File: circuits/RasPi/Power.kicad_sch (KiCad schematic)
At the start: 81 parts, among them IC1 DCDC_MPM3620A, J10 Conn_01x02_Male, J11 Conn_01x02_Male, J12 Conn_01x02_Male, J13 Conn_01x02_Male, J6 USB_C_Receptacle_USB2.0, J9 Conn_01x02_Male, Q16 SSM6J808R, Q17 SSM6J808R, Q18 SSM3J332R, Q19 S8550, Q2 BSS138, Q20 SSM3J332R, Q21 S8550, Q23 S8550, Q24 SSM3J332R, Q25 S8550, Q3 SSM3J332R, Q4 BSS138, SW1 SW_SPDT_White

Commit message: 無線&UI完成？
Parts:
- added J12, J13, J14: Conn_01x02_Male, Connector_Molex:Molex_SPOX_5267-02A_1x02_P2.50mm_Vertical, symbol Connector:Conn_01x02_Male
- renumbered C40 to C19, C1 to C20, C23 to C21, C2 to C22, C3 to C23, C4 to C24, C5 to C25, C32 to C26, C6 to C27, C33 to C28, C23 to C29, C8 to C30, C37 to C31, C25 to C32, C38 to C33, C26 to C34, C39 to C35, D5 to D10, D6 to D11, D1 to D4, D8 to D5, D2 to D6, D3 to D7, D4 to D8, J12 to J10, J13 to J11, J9 to J7, J10 to J8, J11 to J9, Q2 to Q10, Q3 to Q11, Q17 to Q12, Q4 to Q13, Q16 to Q14, Q23 to Q15, Q24 to Q16, Q25 to Q17, Q18 to Q6, Q19 to Q7, Q20 to Q8, Q21 to Q9, R64 to R42, R65 to R43, R76 to R44, R3 to R45, R91 to R46, R92 to R47, R93 to R48, R94 to R49, R4 to R50, R5 to R51, R6 to R52, R95 to R53, R8 to R54, R96 to R55, R7 to R56, R10 to R57, R9 to R58, R11 to R59, R1 to R60, R12 to R61, R2 to R62, R99 to R63, R13 to R64, R100 to R65, R14 to R66, R15 to R67, R16 to R68, R17 to R69, R18 to R70, R19 to R71, R20 to R72, R65 to R73, SW1 to SW4, TP3 to TP1, TP1 to TP2, TP2 to TP3
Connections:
- net +BATT: now also J12.2 (Pin_2), J13.2 (Pin_2), J14.2 (Pin_2)
- net GND: now also J12.1 (Pin_1), J13.1 (Pin_1), J14.1 (Pin_1)
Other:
- note added: "三端子を新しく選定したのにする"
- note removed: "三端子を新しく選定したのにする 電源直付けのための穴を設定する 電源平滑コンデンサは基板設計の時に良い感じに数調整"

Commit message: ラズパイ基板とか
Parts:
- removed C26, C28, C31, C33, C35: 470uF, symbol Device:C_Polarized
- removed J10, J11, J12, J13, J14, J7, J8, J9: Conn_01x02_Male, Connector_Molex:Molex_SPOX_5267-02A_1x02_P2.50mm_Vertical, symbol Connector:Conn_01x02_Male
- R71, R72, R73: value 2k -> 1k
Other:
- note removed: "Conn to EachBoard"
- note removed: "Conn to Power"

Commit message: PDFプロット
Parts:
- removed IC1: DCDC_MPM3620A, MyLibrary:DCDC_MPM3620A, symbol MyLibrary:DCDC_MPM3620A
- removed Q11: SSM3J332R, Package_TO_SOT_SMD:SOT-23W, symbol Device:Q_PMOS_GSD
- added C47: 4700pF, Capacitor_SMD:C_0603_1608Metric, symbol Device:C
- added C48, C50: 47uF, Capacitor_SMD:C_0805_2012Metric, symbol Device:C
- added C49: 100uF, Capacitor_SMD:C_0805_2012Metric, symbol Device:C
- added C51: 0.1uF, Capacitor_SMD:C_0603_1608Metric, symbol Device:C
- added C52: 0.1uF, Capacitor_SMD:C_0402_1005Metric, symbol Device:C
- added D16, D18: D_Zener, Diode_SMD:D_SOD-323_HandSoldering, symbol Device:D_Zener
- added D17, D19: SS2040FL, Diode_SMD:D_SOD-123, symbol Device:D_Schottky
- added J4: Conn_01x02_Pin, symbol Connector:Conn_01x02_Pin
- added L2, L3: 2.2uH, MyLibrary:Inductor_CDPH4D19F, symbol Device:L
- added R119: 200k, Resistor_SMD:R_0402_1005Metric, symbol Device:R
- added R121: 53.6k, Resistor_SMD:R_0402_1005Metric, symbol Device:R
- added R122: 10k, Resistor_SMD:R_0402_1005Metric, symbol Device:R
- added U13: TPS54560BDDA, Package_SO:Texas_R-PDSO-G8_EP2.95x4.9mm_Mask2.4x3.1mm_ThermalVias, symbol Regulator_Switching:TPS54560BDDA
- added U15: TPS61022, Package_DFN_QFN:Texas_RWU0007A_VQFN-7_2x2mm_P0.5mm, symbol Converter_DCDC:TPS61022
- added U16: AZ1084CD-3.3, Package_TO_SOT_SMD:TO-252-2, symbol Regulator_Linear:AMS1117CD-3.3
- added U17: M51957B, Package_SO:SOP-8_3.9x4.9mm_P1.27mm, symbol Voltage_Supervisor:M51957B
- C20: value 10uF -> 47uF; footprint Capacitor_SMD:C_1206_3216Metric -> Capacitor_SMD:C_0805_2012Metric
- C22: value 22uF -> 1uF; footprint Capacitor_SMD:C_0805_2012Metric -> Capacitor_SMD:C_0603_1608Metric
- R45: value 200k -> 10k
- R50: value 100k -> 10k
- R51: value 12k -> 53.6k
- R52: value 2.2k -> 10k
- R54: value 10k -> 75k; footprint Resistor_SMD:R_0402_1005Metric -> Resistor_SMD:R_0603_1608Metric
- R57: value 10k -> 5.1k; footprint Resistor_SMD:R_0402_1005Metric -> Resistor_SMD:R_0603_1608Metric
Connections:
- net +3.3V: now also U16.2 (VO)
- net +5V: now also C52.2, U16.3 (VI), U17.7 (VCC)
- net GND: now also R57.2, C47.1, C48.2, C49.2, C50.2, C52.1, D17.2 (A), D18.2 (A), J4.1 (Pin_1), R119.1, R122.1, U13.7 (GND), U13.9 (GND), U15.1 (GND), U16.1 (GND), U17.4 (GND); no longer Q10.2 (S), R57.1
- net VCC: now also C50.1, U13.2 (VIN); no longer C20.1, R45.2
- net VDD: now also R54.2
- net VSYS: now also C22.1, D4.2 (A), Q10.3 (D), R50.2, R51.2, C48.1, C49.1, D19.1 (K), L2.2, R121.2, U15.3 (VOUT), U15.5 (EN), U15.7 (VIN); no longer R57.2
- net Vout: no longer C22.1, D4.2 (A), R51.2, R54.1
- net FB_Boost: now reaches R51.1, R52.2
- net FB_Boost: now also U15.4 (FB)
- net at R45.1: now also Q10.2 (S)
- net PG: no longer names the net of Q10.1 (G), R50.1
- net PG: now also D16.1 (K), D18.1 (K)
- new net: R54.1, R57.1, U17.2 (IN)
- new net: C47.2, U17.5 (Cdelay)
- new net: C51.2, D17.1 (K), L2.1, U13.8 (SW)
- new net: L3.1, U15.2 (SW)
- new net: C51.1, U13.1 (BOOT)
- new net: R119.2, U13.4 (RT/CLK)
- new net Cap: C20.1, D16.2 (A), D19.2 (A), J4.2 (Pin_2), L3.2, R45.2
- new net FB_Buck: R121.1, R122.2, U13.5 (FB)
- new net UV_SHDN: U17.6 (OUT)
- no-connect marks 11 -> 9
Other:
- note added: "定電流回路"
- note added: "昇圧回路"
- note added: "電圧監視"
- note added: "電気二重層キャパシタへ"
- moved on the sheet: C19, C21, C23, C24, C25, C27, C29, C30, C32, C34, D10, D11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

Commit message: panelフットプリント配置
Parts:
- removed C19: 10uF, Capacitor_SMD:C_0805_2012Metric, symbol Device:C
- removed C20, C48: 47uF, Capacitor_SMD:C_0805_2012Metric, symbol Device:C
- removed C22: 1uF, Capacitor_SMD:C_0603_1608Metric, symbol Device:C
- removed D19: SS2040FL, Diode_SMD:D_SOD-123, symbol Device:D_Schottky
- removed J6: USB_C_Receptacle_USB2.0, Connector_USB:USB_C_Receptacle_G-Switch_GT-USB-7010ASV, symbol Connector:USB_C_Receptacle_USB2.0
- removed L3: 2.2uH, MyLibrary:Inductor_CDPH4D19F, symbol Device:L
- removed R42, R43: 5.1k, Resistor_SMD:R_0402_1005Metric, symbol Device:R
- removed R51: 53.6k, Resistor_SMD:R_0402_1005Metric, symbol Device:R
- removed R52: 10k, Resistor_SMD:R_0402_1005Metric, symbol Device:R
- removed U15: TPS61022, Package_DFN_QFN:Texas_RWU0007A_VQFN-7_2x2mm_P0.5mm, symbol Converter_DCDC:TPS61022
- added C55, C57: 47uF, Capacitor_SMD:C_0805_2012Metric, symbol Device:C
- added C56: 1uF, Capacitor_SMD:C_0603_1608Metric, symbol Device:C
- added D27: SS2040FL, Diode_SMD:D_SOD-123, symbol Device:D_Schottky
- added L4: 2.2uH, MyLibrary:Inductor_CDPH4D19F, symbol Device:L
- added R100: 10k, Resistor_SMD:R_0402_1005Metric, symbol Device:R
- added R99: 53.6k, Resistor_SMD:R_0402_1005Metric, symbol Device:R
- added U19: DCDC_TPS61023, MyLibrary:DCDC_TPS61023, symbol MyLibrary:DCDC_TPS61023
- U16: value AZ1084CD-3.3 -> AZ1117CH-3.3; footprint Package_TO_SOT_SMD:TO-252-2 -> Package_TO_SOT_SMD:SOT-223-3_TabPin2
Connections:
- net Cap: now also C55.1, D27.2 (A), L4.2
- net FB_Boost: now also R100.2, R99.1, U19.1 (FB)
- net GND: now also C55.2, C56.2, C57.2, R100.1, U19.4 (GND)
- net VSYS: now also C56.1, C57.1, D27.1 (K), R99.2, U19.2 (EN), U19.3 (VIN), U19.6 (VOUT)
- new net: L4.1, U19.5 (SW)
- no-connect marks 9 -> 3
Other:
- note added: "三端子を新しく選定したのにする 昇圧回路のFB電圧をちょっと低く設定する"
- note removed: "USB-C"
- note removed: "三端子を新しく選定したのにする"
- moved on the sheet: C21, C24, C25, C47, C52, D5, D8, Q6, Q7, Q8, Q9, R44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

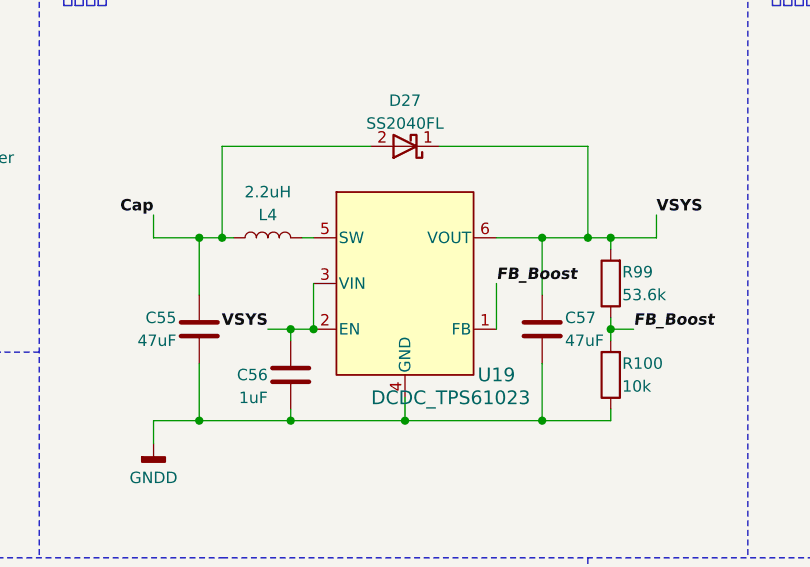
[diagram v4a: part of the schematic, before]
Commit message: シンボル・フットプリントMyLib->TomoshibiLib置き換え
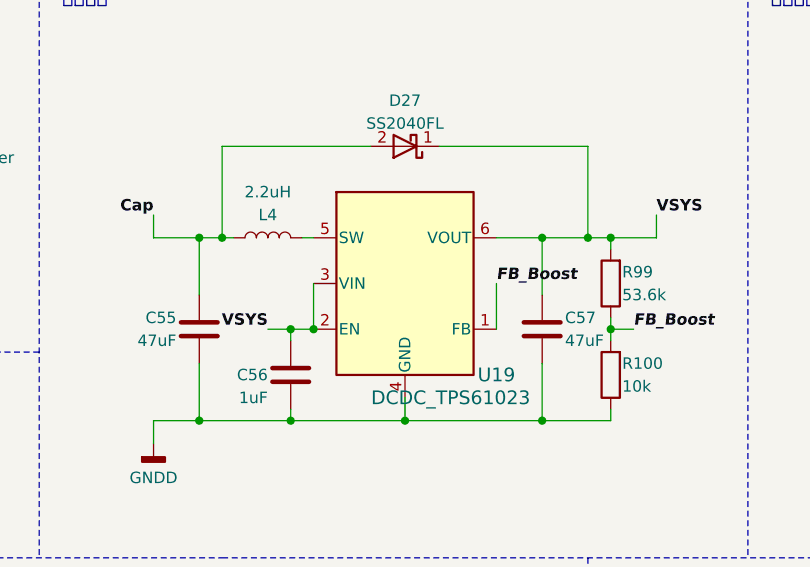
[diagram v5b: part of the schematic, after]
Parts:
- L1: footprint MyLibrary:Inductor_CDPH4D19F -> TomoshibiLibrary:Inductor_CDPH4D19F
- L2, L4: footprint MyLibrary:Inductor_CDPH4D19F -> (none)
- Q12, Q14: footprint MyLibrary:Package_TSOP6F -> TomoshibiLibrary:Package_TSOP6F
- SW4: footprint MyLibrary:SW_Slide_SPDT_White -> TomoshibiLibrary:SW_Slide_SPDT_White
- U17: symbol Voltage_Supervisor:M51957B -> TomoshibiLibrary:Power_Supervisor_M51957B
- U19: footprint MyLibrary:DCDC_TPS61023 -> TomoshibiLibrary:DCDC_TPS61023; symbol MyLibrary:DCDC_TPS61023 -> TomoshibiLibrary:DCDC_TPS61023
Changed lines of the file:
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@@
       (effects (font (size 1.27 1.27)))
     )
-    (property "Footprint" "MyLibrary:Inductor_CDPH4D19F" (at 129.54 71.12 0)
+    (property "Footprint" "TomoshibiLibrary:Inductor_CDPH4D19F" (at 129.54 71.12 0)
       (effects (font (size 1.27 1.27)) hide)
     )
@@
       (effects (font (size 1.27 1.27)))
     )
-    (property "Footprint" "MyLibrary:Inductor_CDPH4D19F" (at 210.82 147.32 0)
+    (property "Footprint" "" (at 210.82 147.32 0)
       (effects (font (size 1.27 1.27)) hide)
     )
@@
     )
   )
-  (symbol (lib_id "MyLibrary:DCDC_TPS61023") (at 226.06 152.4 0) (unit 1)
+  (symbol (lib_id "TomoshibiLibrary:DCDC_TPS61023") (at 226.06 152.4 0) (unit 1)
     (in_bom yes) (on_board yes) (dnp no)
     (property "Reference" "U19" (at 236.22 162.56 0)
@@
       (effects (font (size 1.524 1.524)))
     )
-    (property "Footprint" "MyLibrary:DCDC_TPS61023" (at 223.52 124.46 0)
+    (property "Footprint" "TomoshibiLibrary:DCDC_TPS61023" (at 223.52 124.46 0)
       (effects (font (size 1.27 1.27) italic) hide)
     )
@@
       (effects (font (size 1.27 1.27)))
     )
-    (property "Footprint" "MyLibrary:SW_Slide_SPDT_White" (at 86.36 40.64 0)
+    (property "Footprint" "TomoshibiLibrary:SW_Slide_SPDT_White" (at 86.36 40.64 0)
       (effects (font (size 1.27 1.27)) hide)
     )
@@
       (effects (font (size 1.27 1.27)))
     )
-    (property "Footprint" "MyLibrary:Inductor_CDPH4D19F" (at 104.14 149.86 0)
+    (property "Footprint" "" (at 104.14 149.86 0)
       (effects (font (size 1.27 1.27)) hide)
     )
@@
       (effects (font (size 1.27 1.27)))
     )
-    (property "Footprint" "MyLibrary:Package_TSOP6F" (at 96.52 68.58 0)
+    (property "Footprint" "TomoshibiLibrary:Package_TSOP6F" (at 96.52 68.58 0)
       (effects (font (size 1.27 1.27)) (justify left) hide)
     )
@@
       (effects (font (size 1.27 1.27)))
     )
-    (property "Footprint" "MyLibrary:Package_TSOP6F" (at 71.12 68.58 0)
+    (property "Footprint" "TomoshibiLibrary:Package_TSOP6F" (at 71.12 68.58 0)
       (effects (font (size 1.27 1.27)) (justify left) hide)
     )
@@
     )
   )
-  (symbol (lib_id "Voltage_Supervisor:M51957B") (at 91.44 215.9 0) (unit 1)
+  (symbol (lib_id "TomoshibiLibrary:Power_Supervisor_M51957B") (at 91.44 215.9 0) (unit 1)
     (in_bom yes) (on_board yes) (dnp no)
     (property "Reference" "U17" (at 99.06 205.74 0)

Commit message: 更新
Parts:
- removed Q10, Q13: BSS138, Package_TO_SOT_SMD:SOT-23, symbol Device:Q_NMOS_GSD
- removed Q16: SSM3J332R, Package_TO_SOT_SMD:SOT-23W, symbol Device:Q_PMOS_GSD
- added Q11: 2N7002, Package_TO_SOT_SMD:SOT-23, symbol Transistor_FET:2N7002
- added Q16: SSM6J808R, Package_SO:TSOP-6_1.65x3.05mm_P0.95mm, symbol Transistor_FET:PMN48XP
- J4: footprint (none) -> Connector_JST:JST_XH_B2B-XH-AM_1x02_P2.50mm_Vertical
- L1: value 22uH -> 1uH; footprint TomoshibiLibrary:Inductor_CDPH4D19F -> Inductor_SMD:L_0603_1608Metric
- Q12, Q14: footprint TomoshibiLibrary:Package_TSOP6F -> Package_SO:TSOP-6_1.65x3.05mm_P0.95mm
- R100: value 10k -> 1.8k; footprint Resistor_SMD:R_0402_1005Metric -> Resistor_SMD:R_0603_1608Metric
- R99: value 53.6k -> 13k; footprint Resistor_SMD:R_0402_1005Metric -> Resistor_SMD:R_0603_1608Metric
- SW4: value SW_SPDT_White -> SW_SPDT
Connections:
- net +5V: now also Q16.1 (D), Q16.2 (D), Q16.5 (D), Q16.6 (D)
- net GND: now also Q11.2 (S)
- net PowerSW: now also Q11.1 (G)
- net VSYS: now also Q16.4 (S)
- net at R61.2: now also Q11.3 (D)
- net at Q17.3 (C), R65.2: now also Q16.3 (G)
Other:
- note added: "スライドスイッチの色分けとか、スイッチの区別を見直す 電源は白スライド"

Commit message: raspi基板回路図
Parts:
- removed C47: 4700pF, Capacitor_SMD:C_0603_1608Metric, symbol Device:C
- removed C56: 1uF, Capacitor_SMD:C_0603_1608Metric, symbol Device:C
- removed D16, D18: D_Zener, Diode_SMD:D_SOD-323_HandSoldering, symbol Device:D_Zener
- removed R45, R50: 10k, Resistor_SMD:R_0402_1005Metric, symbol Device:R
- added C10, C16, C17: 10uF, Capacitor_SMD:C_1206_3216Metric, symbol Device:C
- added C18, C26, C66, C67, C9: 100uF, Capacitor_SMD:C_1206_3216Metric, symbol Device:C
- added C65: 4.7nF, Capacitor_SMD:C_0402_1005Metric, symbol Device:C
- added C68, C71: 10uF, Capacitor_SMD:C_0805_2012Metric, symbol Device:C
- added C69: C, Resistor_SMD:R_0603_1608Metric, symbol Device:C
- added C70: 15pF, Capacitor_SMD:C_0402_1005Metric, symbol Device:C
- added Q31: MTP4835I3, Package_TO_SOT_SMD:TO-252-2, symbol Device:Q_PMOS_GDS
- added R116: 22k, Resistor_SMD:R_0402_1005Metric, symbol Device:R
- added R124: 100k, Resistor_SMD:R_0402_1005Metric, symbol Device:R
- added R125: 0.1, symbol Device:R
- added R126, R127: R, Resistor_SMD:R_0603_1608Metric, symbol Device:R
- added R128: 200, Resistor_SMD:R_0402_1005Metric, symbol Device:R
- added R129: 5.1k, Resistor_SMD:R_0402_1005Metric, symbol Device:R
- added R43: 2k, Resistor_SMD:R_0402_1005Metric, symbol Device:R
- added U21: 74AHC1G02, Package_TO_SOT_SMD:SOT-23-5, symbol 74xGxx:74AHC1G02
- added U22: NJM2732, symbol Amplifier_Operational:LM7332
- C49: footprint Capacitor_SMD:C_0805_2012Metric -> Capacitor_SMD:C_1206_3216Metric
- C50: value 47uF -> 15pF; footprint Capacitor_SMD:C_0805_2012Metric -> Capacitor_SMD:C_0402_1005Metric
- C51: footprint Capacitor_SMD:C_0603_1608Metric -> Capacitor_SMD:C_0402_1005Metric
- C55: value 47uF -> 10uF
- C57: value 47uF -> 10nF; footprint Capacitor_SMD:C_0805_2012Metric -> Capacitor_SMD:C_0402_1005Metric
- D17: value SS2040FL -> MA10EB045; footprint Diode_SMD:D_SOD-123 -> Diode_SMD:Vishay_SMPA
- L2: value 2.2uH -> 3.3uH; footprint (none) -> TomoshibiLibrary:Inductor_ECS-MPIL0530
- L4: value 2.2uH -> 1uH; footprint (none) -> Inductor_SMD:L_1210_3225Metric
- R119: value 200k -> 100k
- R121: value 53.6k -> 22k
- R122: value 10k -> 2.2k
- R54: value 75k -> 100k
- R57: value 5.1k -> 7.5k
- SW4: footprint TomoshibiLibrary:SW_Slide_SPDT_White -> TomoshibiLibrary:SW_Slide_SPDT_IS-1235-G
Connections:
- net Cap: now also C55.2, U19.3 (VIN), C68.2, Q31.2 (D), R124.2; no longer C55.1
- net FB_Boost: now also C57.2
- net FB_Buck: now also R43.2; no longer R122.2
- net GND: now also C55.1, R122.2, C10.2, C16.2, C17.2, C18.2, C26.2, C65.2, C66.2, C67.2, C68.1, C70.2, C71.1, C9.2, R129.1, U22.4 (V-), U22.5 (+), U22.6 (-); no longer C55.2, C57.2, R122.1
- net VCC: now also C10.1, C16.1, C17.1; no longer C50.1
- net VSYS: now also C18.1, C26.1, C66.1, C67.1, C71.2, C9.1, R125.1, R128.2, U22.8 (V+); no longer U19.2 (EN), U19.3 (VIN)
- net at U17.5 (Cdelay): now also C70.1
- net at U13.6 (COMP): now also C50.1, R116.2
- new net: C65.1, R116.1
- new net: C69.1, R126.2, U22.1
- new net: C69.2, R127.2, U22.2 (-)
- new net: R128.1, R129.2, U22.3 (+)
- new net: Q31.1 (G), R126.1
- new net: Q31.3 (S), R125.2, R127.1
- new net: R122.1, R43.1
- new net EN_Boost: R124.1, U19.2 (EN)
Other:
- note added: "ダイオード変更"
- note removed: "スライドスイッチの色分けとか、スイッチの区別を見直す 電源は白スライド"
- note removed: "三端子を新しく選定したのにする 昇圧回路のFB電圧をちょっと低く設定する"
- note removed: "電源スイッチ 耐圧大丈夫？"
- moved on the sheet: C21, C23, C24, C25, C27, C29, C30, C32, C34, C51, C52, D10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
